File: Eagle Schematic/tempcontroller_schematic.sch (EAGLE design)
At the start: 13 parts, among them T1 2N2222

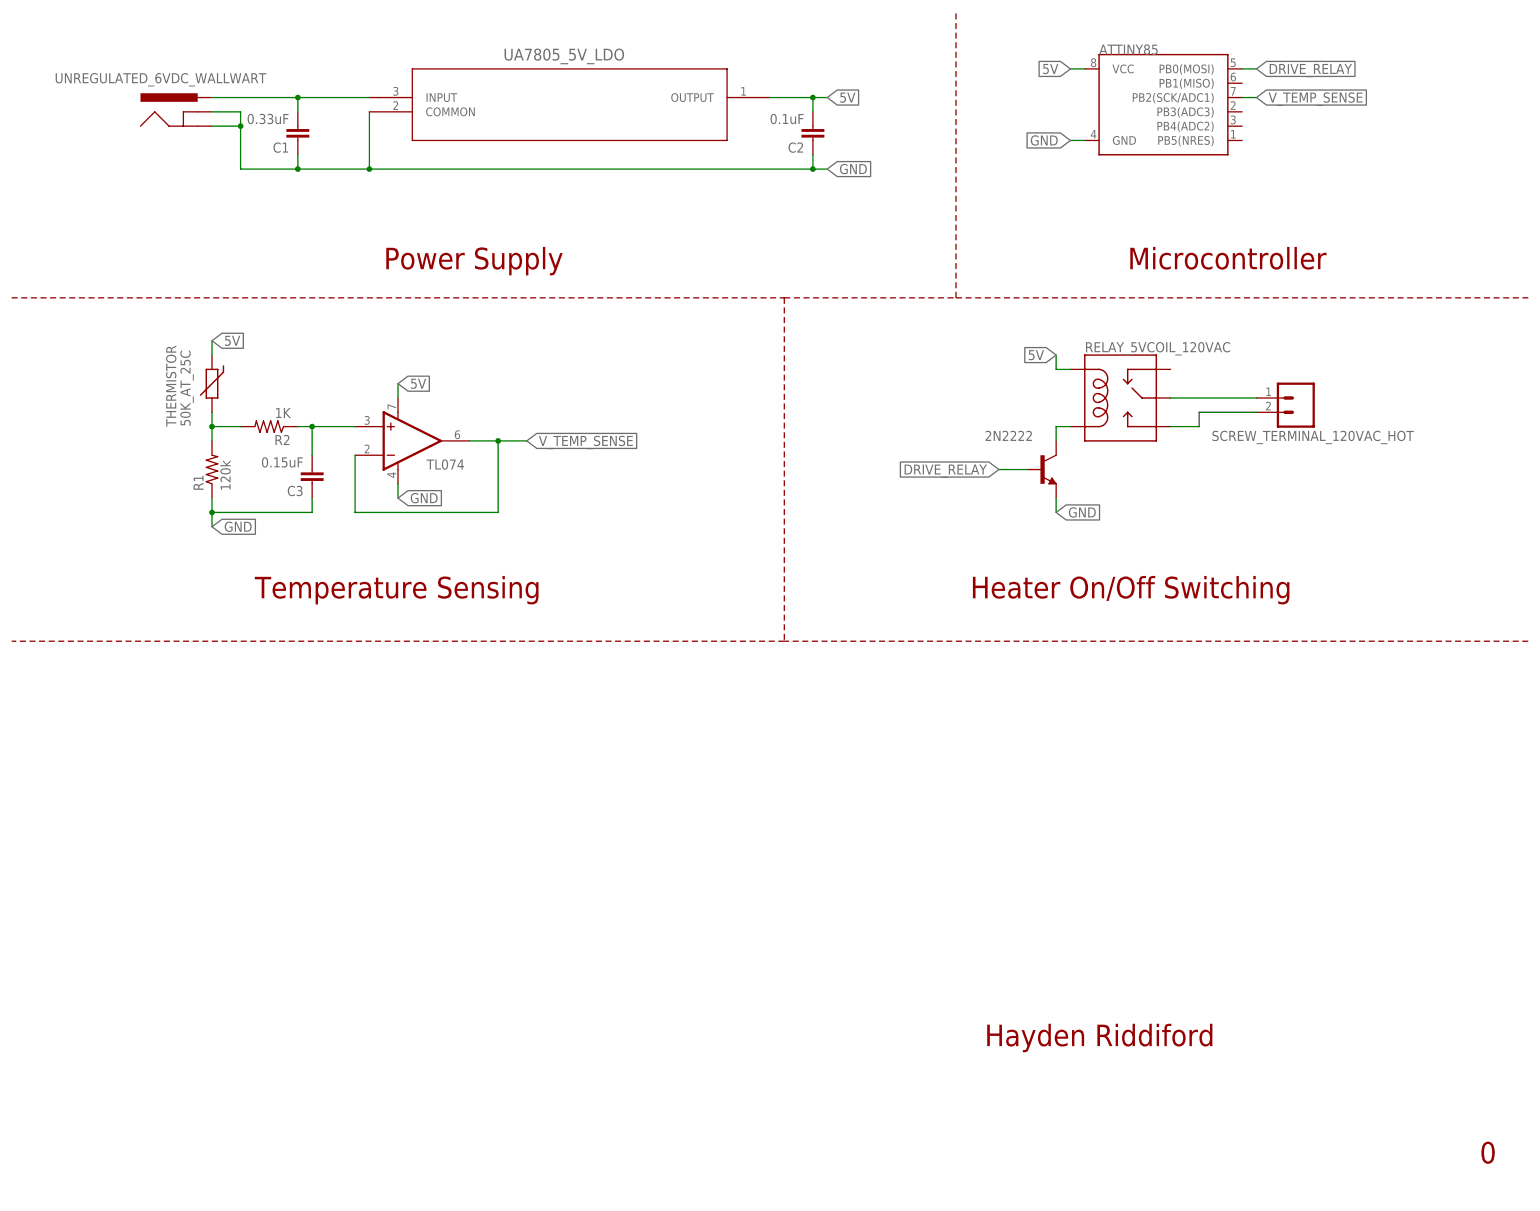
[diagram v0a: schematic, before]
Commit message: Added temperature control potentiometer
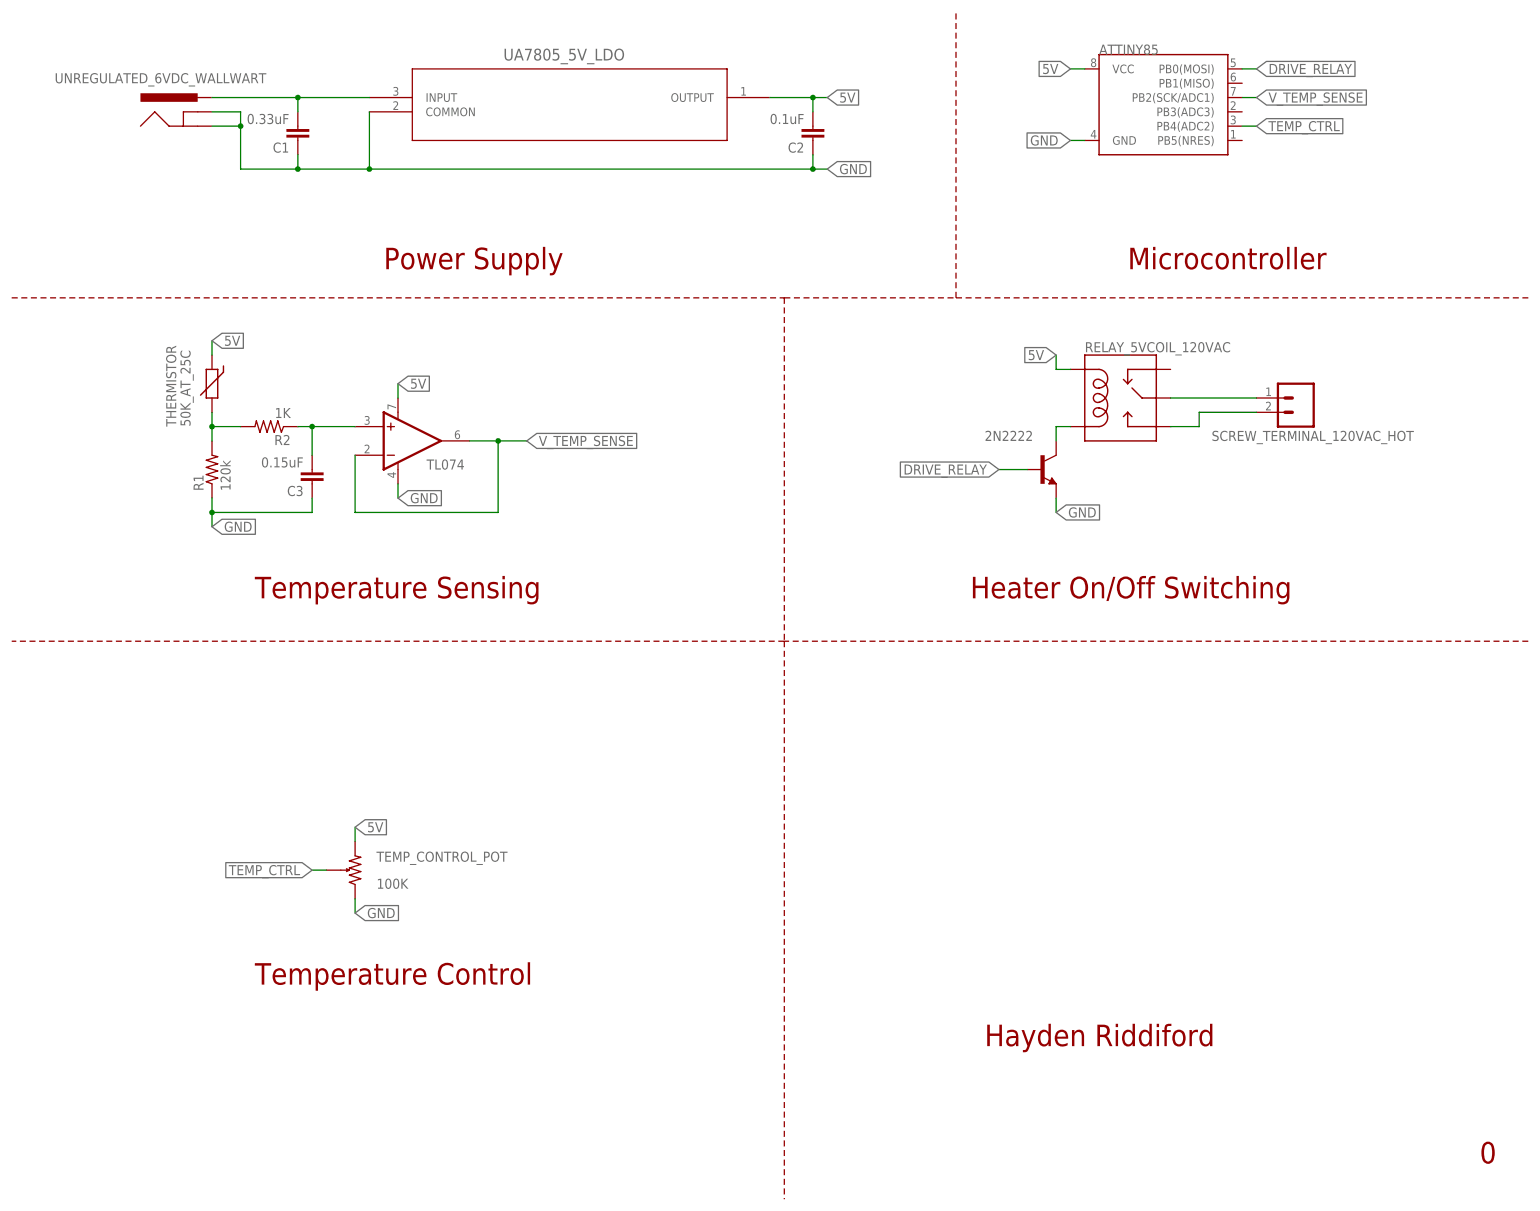
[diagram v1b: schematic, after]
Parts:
- added TEMP_CONTROL_POT: 100K, SparkFun-Passives:POTENTIOMETER
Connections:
- new net TEMP_CTRL: ATTINY85.PB4(ADC2), TEMP_CONTROL_POT.P$1
- net 5V: now also TEMP_CONTROL_POT.2
- net GND: now also TEMP_CONTROL_POT.1
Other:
- note added: "Temperature Control"
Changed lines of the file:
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@@
 <part name="SCREW_TERMINAL_120VAC_HOT" library="SparkFun-Connectors" deviceset="M02" device="POLAR"/>
 <part name="FRAME2" library="frames" deviceset="FRAME_A_L" device=""/>
+<part name="TEMP_CONTROL_POT" library="SparkFun-Passives" deviceset="POTENTIOMETER" device="" value="100K"/>
 </parts>
 <sheets>
@@
 <text x="53.34" y="-107.442" size="3.81" layer="94" font="vector">Hayden Riddiford</text>
 <text x="141.224" y="-128.27" size="3.81" layer="94" font="vector">0</text>
+<text x="-76.2" y="-96.52" size="3.81" layer="94">Temperature Control</text>
+<wire x1="17.78" y1="-35.56" x2="17.78" y2="-134.62" width="0.1524" layer="94" style="shortdash"/>
 </plain>
 <instances>
@@
 <instance part="FRAME2" gate="G$1" x="-124.46" y="-134.62"/>
 <instance part="FRAME2" gate="G$2" x="48.26" y="-134.62"/>
+<instance part="TEMP_CONTROL_POT" gate="G$1" x="-58.42" y="-76.2" smashed="yes" rot="R90">
+<attribute name="NAME" x="-54.61" y="-74.7014" size="1.778" layer="95"/>
+<attribute name="VALUE" x="-54.61" y="-79.502" size="1.778" layer="96"/>
+</instance>
 </instances>
 <busses>
@@
 <wire x1="71.12" y1="66.04" x2="68.58" y2="66.04" width="0.1524" layer="91"/>
 <label x="68.58" y="66.04" size="1.778" layer="95" rot="R180" xref="yes"/>
+</segment>
+<segment>
+<pinref part="TEMP_CONTROL_POT" gate="G$1" pin="2"/>
+<wire x1="-58.42" y1="-71.12" x2="-58.42" y2="-68.58" width="0.1524" layer="91"/>
+<label x="-58.42" y="-68.58" size="1.778" layer="95" xref="yes"/>
 </segment>
 </net>
@@
 <label x="68.58" y="53.34" size="1.778" layer="95" rot="R180" xref="yes"/>
 </segment>
+<segment>
+<pinref part="TEMP_CONTROL_POT" gate="G$1" pin="1"/>
+<wire x1="-58.42" y1="-81.28" x2="-58.42" y2="-83.82" width="0.1524" layer="91"/>
+<label x="-58.42" y="-83.82" size="1.778" layer="95" xref="yes"/>
+</segment>
 </net>
 <net name="N$1" class="0">
@@
 </segment>
 </net>
+<net name="TEMP_CTRL" class="0">
+<segment>
+<pinref part="ATTINY85" gate="G$1" pin="PB4(ADC2)"/>
+<wire x1="99.06" y1="55.88" x2="101.6" y2="55.88" width="0.1524" layer="91"/>
+<label x="101.6" y="55.88" size="1.778" layer="95" xref="yes"/>
+</segment>
+<segment>
+<pinref part="TEMP_CONTROL_POT" gate="G$1" pin="P$1"/>
+<wire x1="-63.5" y1="-76.2" x2="-66.04" y2="-76.2" width="0.1524" layer="91"/>
+<label x="-66.04" y="-76.2" size="1.778" layer="95" rot="R180" xref="yes"/>
+</segment>
+</net>
